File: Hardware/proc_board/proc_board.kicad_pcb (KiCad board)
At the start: 2 copper layers, 80.8 x 60.1 mm, 18 parts, among them J1 Conn_01x40, U1 74HC21, U2 W65C02SxP, U3 HM62256BLP, U4 28C256, U5 74HC00, U6 HM62256BLP

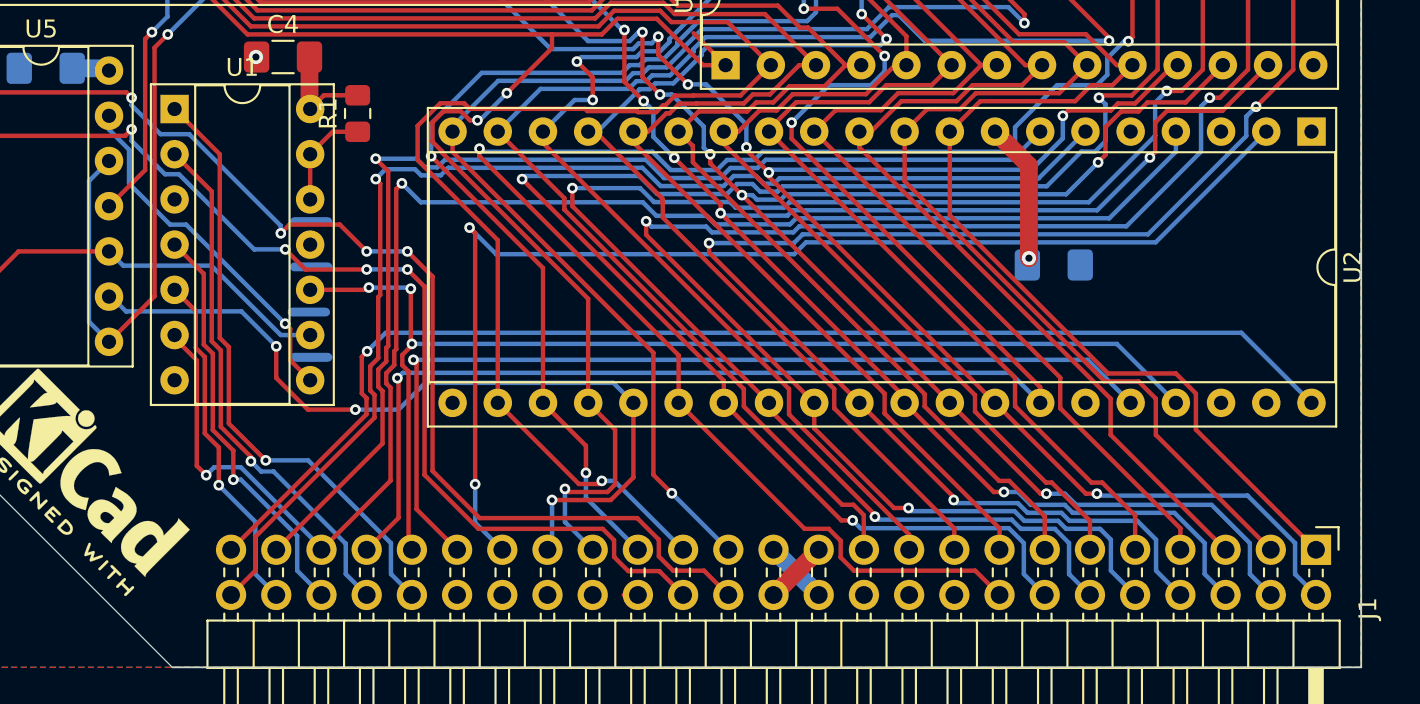
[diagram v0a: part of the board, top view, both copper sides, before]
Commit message: Add clock stretching with counter and slow clock request from peripherals.
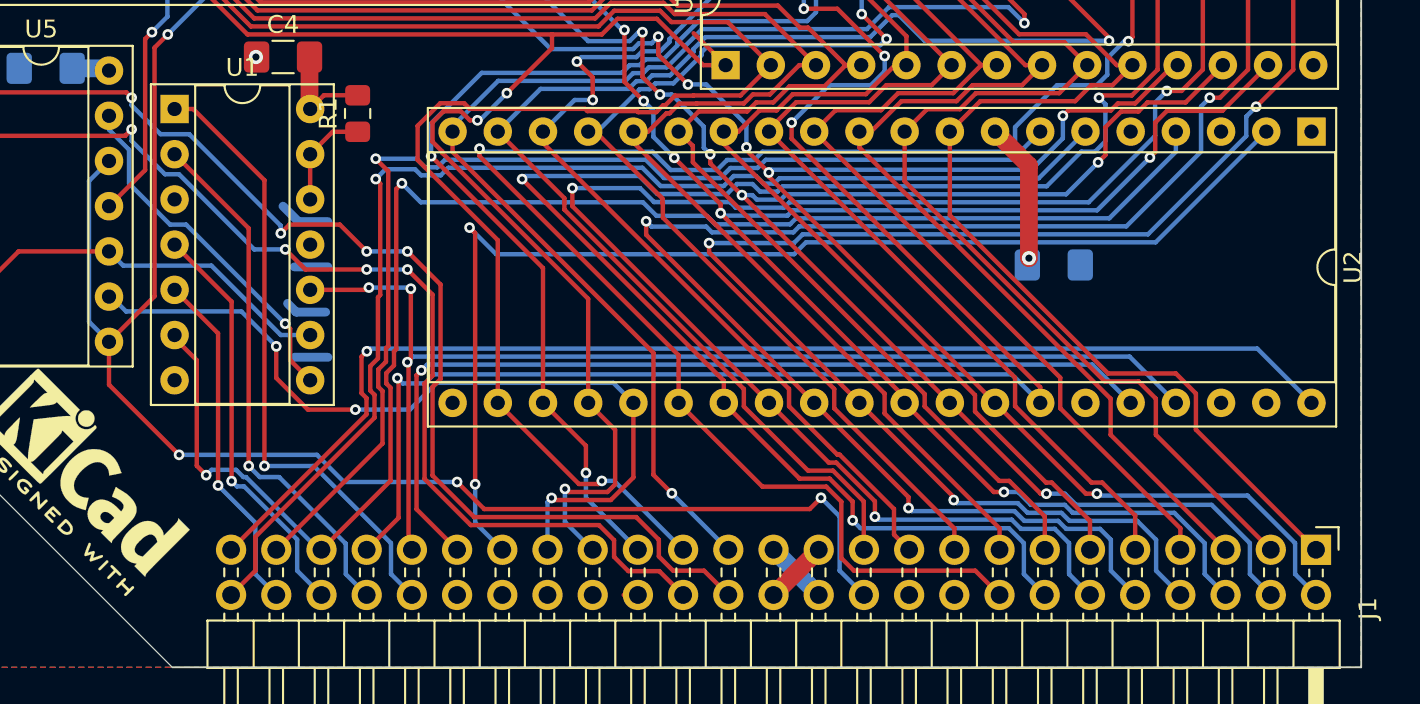
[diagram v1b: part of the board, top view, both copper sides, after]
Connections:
- J1 pad 22: EX2 -> ROM_CS
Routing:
- net ROM_CS: track 54.3 -> 106.3 mm, vias 3 -> 6
- net GND: track 11.1 -> 12.6 mm
- net D7: track 143.6 -> 144.9 mm
- net BE: track 53.0 -> 52.0 mm
- net ~IRQ3~: track 34.2 -> 35.1 mm
- net ~RESET~: track 69.7 -> 68.9 mm
- net D6: track 144.9 -> 145.5 mm
- net ~SSEL~: track 62.5 -> 63.0 mm
- net ~INH~: track 58.5 -> 59.0 mm

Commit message: Many updates. SLOW signal is now shared amongst all slots, so their output has to be open drain.
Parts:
- added D1: D_Schottky, Diode_SMD:D_0805_2012Metric_Pad1.15x1.40mm_HandSolder, F.Cu at (13.1, -13.4)
- added R2: 1k, Resistor_SMD:R_0805_2012Metric_Pad1.15x1.40mm_HandSolder, F.Cu at (13.2, -10.4)
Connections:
- J1 pad 22: ROM_CS -> ~SLOW~
- U4 pad 20: ROM_CS -> GND
- U4 pad 22: GND -> ROM_CS
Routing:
- net ROM_CS: track 106.3 -> 59.1 mm, vias 6 -> 3
- net ~SLOW~: track 0.00 -> 47.1 mm, vias 0 -> 3
- net GND: track 12.6 -> 8.36 mm

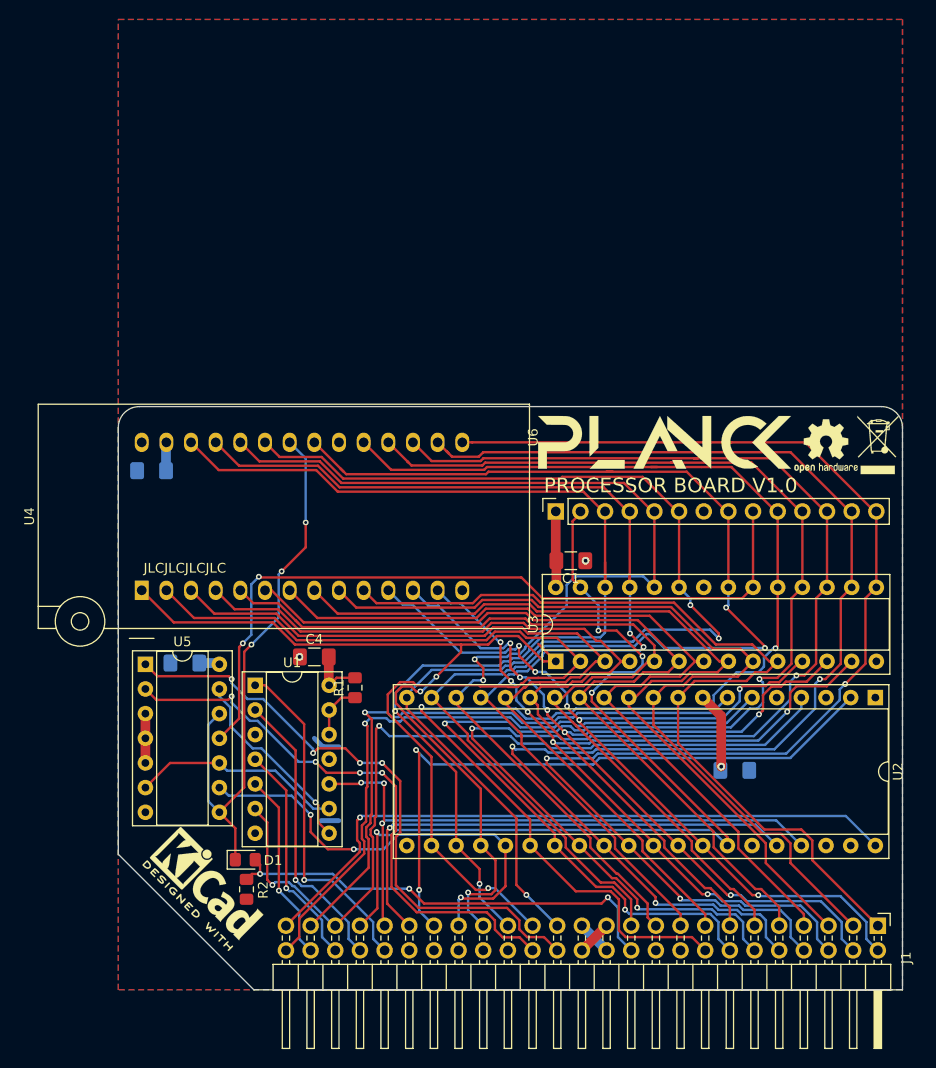
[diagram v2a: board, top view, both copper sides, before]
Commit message: update CPU board address decoding with a 16V8
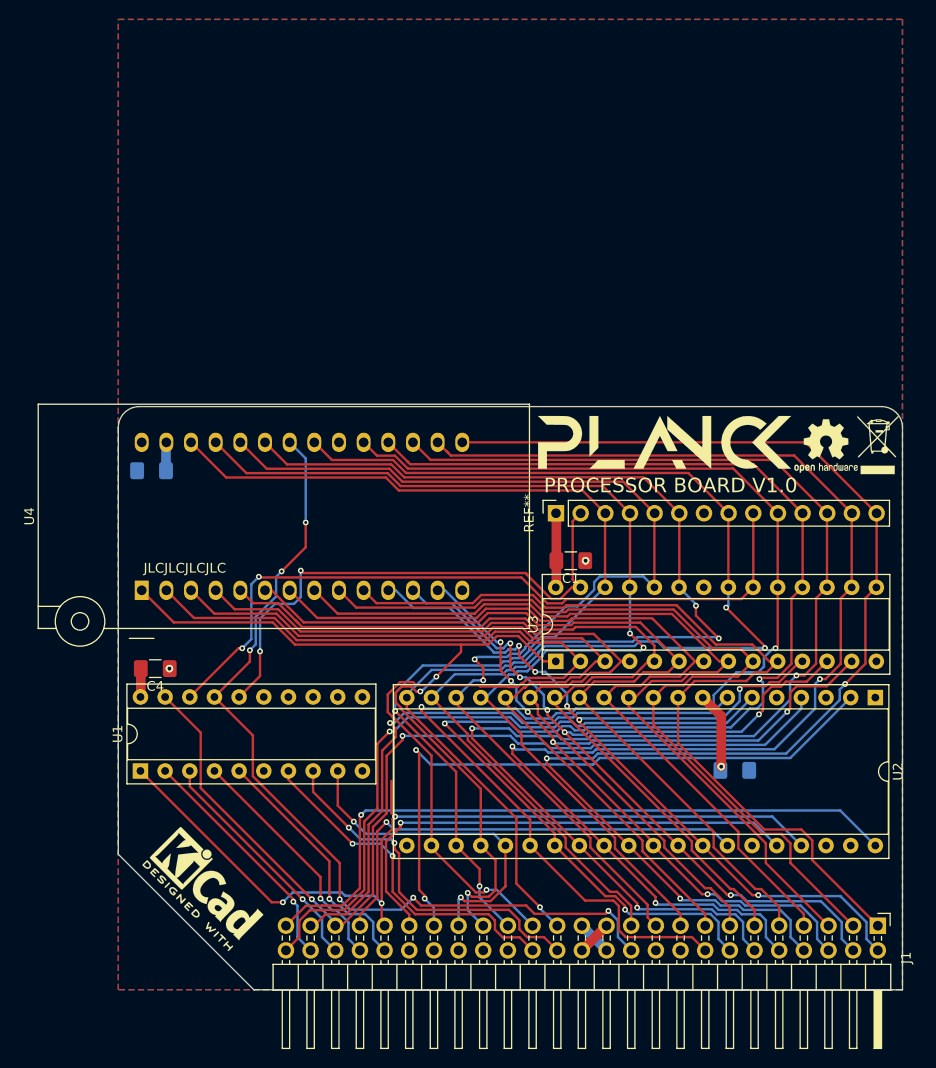
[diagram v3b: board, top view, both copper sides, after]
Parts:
- removed C2: C_Small, Capacitor_SMD:C_1206_3216Metric_Pad1.42x1.75mm_HandSolder
- removed D1: D_Schottky, Diode_SMD:D_0805_2012Metric_Pad1.15x1.40mm_HandSolder
- removed R1: 4k7, Resistor_SMD:R_0805_2012Metric_Pad1.15x1.40mm_HandSolder
- removed R2: 1k, Resistor_SMD:R_0805_2012Metric_Pad1.15x1.40mm_HandSolder
- removed U5: 74HC00, Package_DIP:DIP-14_W7.62mm_Socket
- removed U6: HM62256BLP, Connector_PinSocket_2.54mm:PinSocket_1x14_P2.54mm_Vertical
- added REF**: PinSocket_1x14_P2.54mm_Vertical, Connector_PinSocket_2.54mm:PinSocket_1x14_P2.54mm_Vertical, F.Cu at (45.1, -49.1)
- U1: value 74HC21 -> GAL16V8; footprint Package_DIP:DIP-14_W7.62mm_Socket -> Package_DIP:DIP-20_W7.62mm_Socket
- moved C4 16.4 mm to (3.81, -33.1), turned to 180 degrees
- moved U1 14.7 mm to (2.29, -22.5), turned to 90 degrees
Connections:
- J1 pad 22: ~SLOW~ -> ~ROM_CS~
- U1 pad 1: ~IRQ3~ -> CLK
- U1 pad 10: CLK -> GND
- U1 pad 11: (no net) -> Net-(U1-Pad11)
- U1 pad 12: Net-(R1-Pad1) -> Net-(U1-Pad12)
- U1 pad 13: Net-(R1-Pad1) -> Net-(U1-Pad13)
- U1 pad 14: +5V -> Net-(U1-Pad14)
- U1 pad 2: ~IRQ2~ -> ~IRQ0~
- U1 pad 3: (no net) -> ~IRQ1~
- U1 pad 4: ~IRQ1~ -> ~IRQ2~
- U1 pad 5: ~IRQ0~ -> ~IRQ3~
- U1 pad 6: ~IRQ~ -> Net-(U1-Pad6)
- U1 pad 7: GND -> ~INH~
- U1 pad 8: Net-(U1-Pad8) -> ~SSEL~
- U1 pad 9: Net-(U1-Pad9) -> A15
- U3 pad 20: RAM_CS -> ~RAM_CS~
- U3 pad 27: R~W~ -> ~RAMW~
- U4 pad 22: ROM_CS -> ~ROM_CS~
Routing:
- net ~ROM_CS~: track 0.00 -> 91.5 mm, vias 0 -> 6
- net RAM_CS: track 78.2 -> 0.00 mm, vias 2 -> 0
- net ~RAM_CS~: track 0.00 -> 75.9 mm, vias 0 -> 2
- net ROM_CS: track 59.1 -> 0.00 mm, vias 3 -> 0
- net ~RAMW~: track 0.00 -> 55.6 mm, vias 0 -> 2
- net R~W~: track 95.5 -> 47.9 mm, vias 4 -> 1
- net ~SLOW~: track 47.1 -> 0.00 mm, vias 3 -> 0
- net ~SSEL~: track 63.0 -> 37.3 mm, vias 4 -> 2
- net CLK: track 65.0 -> 90.2 mm
- net ~INH~: track 59.0 -> 36.0 mm, vias 4 -> 2
- net Net-(U1-Pad9): track 21.9 -> 0.00 mm
- net Net-(U1-Pad8): track 20.1 -> 0.00 mm, vias 1 -> 0
- net A15: track 46.6 -> 35.1 mm, vias 3 -> 2
- net ~IRQ~: track 87.0 -> 98.0 mm
- net ~IRQ3~: track 35.1 -> 25.9 mm
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
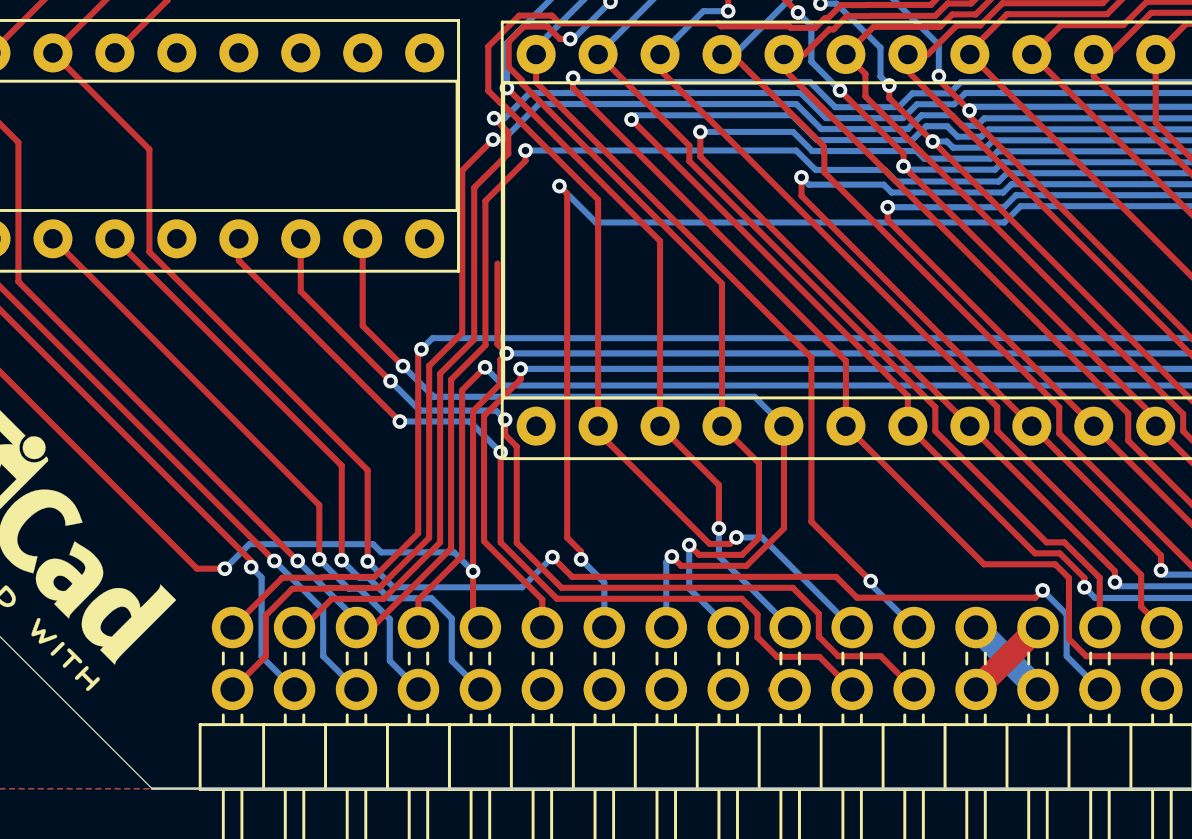
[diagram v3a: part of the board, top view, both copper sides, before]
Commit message: Add IRQ signal for Slot 5
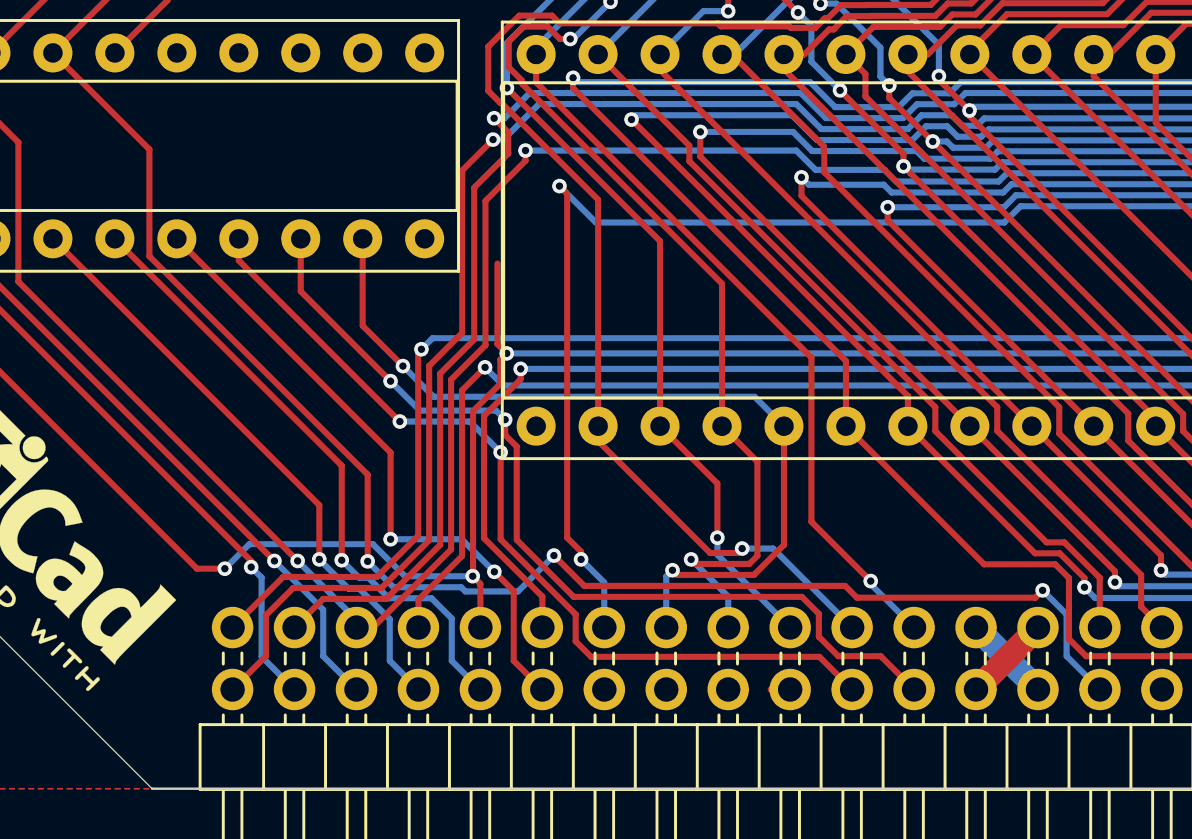
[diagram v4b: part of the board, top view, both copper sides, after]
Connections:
- J1 pad 40: LED4 -> ~IRQ5~
- J1 pad 42: ~IRQ3~ -> ~IRQ4~
- J1 pad 44: ~IRQ2~ -> ~IRQ3~
- J1 pad 46: ~IRQ1~ -> ~IRQ2~
- J1 pad 48: ~IRQ0~ -> ~IRQ1~
- U1 pad 2: ~IRQ0~ -> ~IRQ1~
- U1 pad 3: ~IRQ1~ -> ~IRQ2~
- U1 pad 4: ~IRQ2~ -> ~IRQ3~
- U1 pad 5: ~IRQ3~ -> ~IRQ4~
- U1 pad 6: Net-(U1-Pad6) -> ~IRQ5~
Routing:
- net ~IRQ5~: track 0.00 -> 26.4 mm, vias 0 -> 2
- net ~IRQ4~: track 0.00 -> 25.9 mm, vias 0 -> 1
- net ~IRQ0~: track 24.7 -> 0.00 mm, vias 1 -> 0
- net ~IRQ3~: track 25.9 -> 24.9 mm

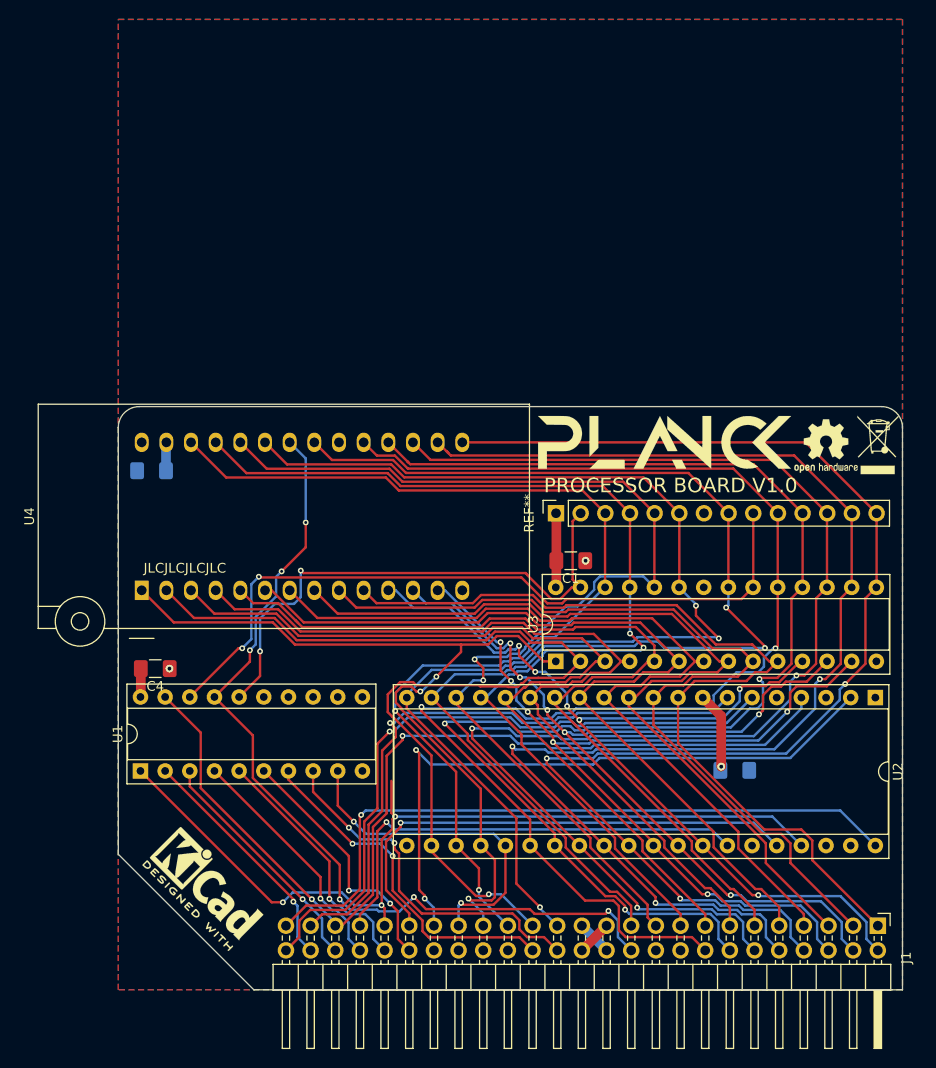
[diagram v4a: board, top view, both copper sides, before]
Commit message: Update processor board according to schematic
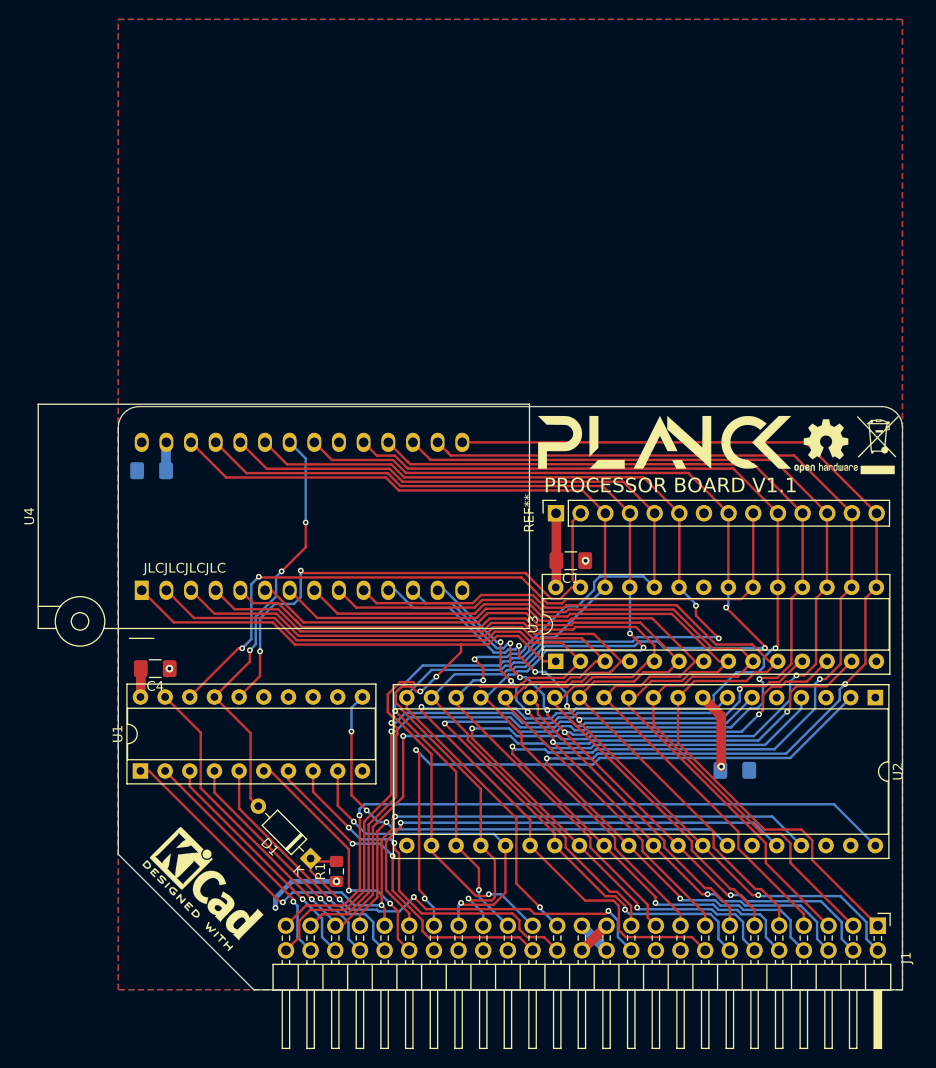
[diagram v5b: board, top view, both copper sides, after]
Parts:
- added D1: 1N4148, Diode_THT:D_DO-35_SOD27_P7.62mm_Horizontal, F.Cu at (19.8, -13.5)
- added R1: 4.7k, Resistor_SMD:R_0805_2012Metric_Pad1.15x1.40mm_HandSolder, F.Cu at (22.5, -12.2)
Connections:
- J1 pad 22: ~ROM_CS~ -> ~SLOW~
- U1 pad 11: Net-(U1-Pad11) -> R~W~
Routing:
- net ~ROM_CS~: track 91.7 -> 44.1 mm, vias 6 -> 3
- net ~SLOW~: track 0.00 -> 43.0 mm, vias 0 -> 3
- net R~W~: track 47.9 -> 63.2 mm, vias 1 -> 3
- net +5V: track 25.1 -> 33.1 mm, vias 1 -> 3
- net CLK: track 90.3 -> 86.4 mm
- net ~RESET~: track 71.5 -> 72.5 mm
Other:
- board text added: "PROCESSOR BOARD V1.1"
- board text removed: "PROCESSOR BOARD V1.0"
